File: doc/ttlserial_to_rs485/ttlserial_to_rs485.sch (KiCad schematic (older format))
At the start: 26 parts, among them J1 serial, J2 DB9_Female, SW1 term_en, U1 NE555, U2 74HC04, U3 MAX485E

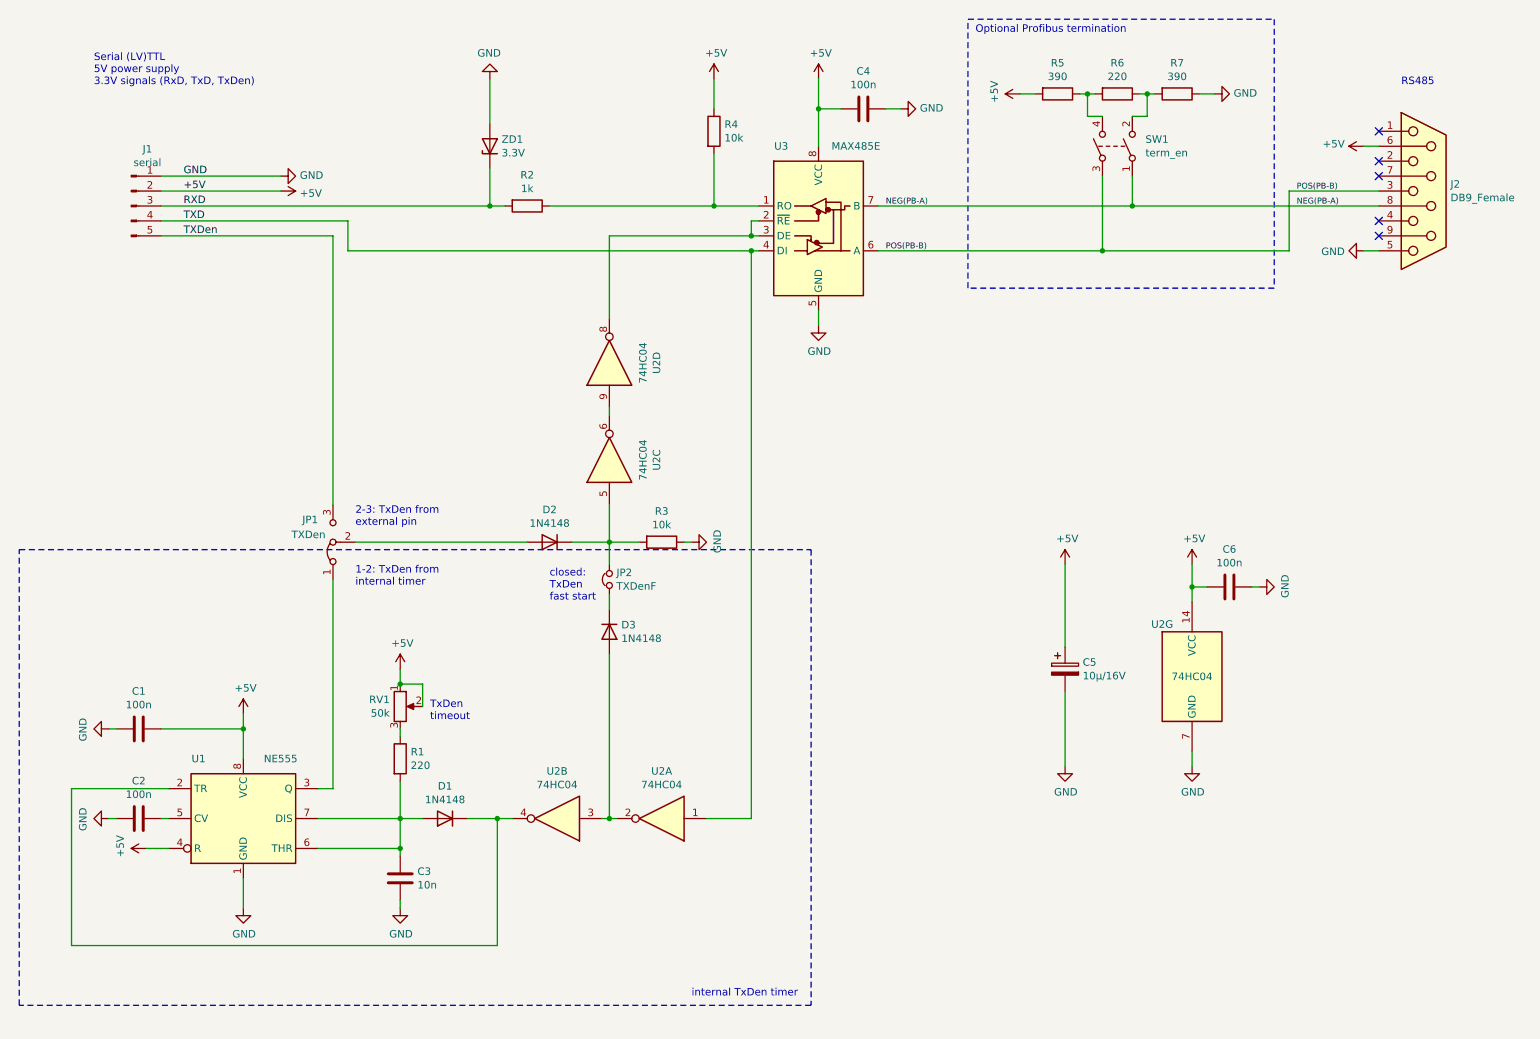
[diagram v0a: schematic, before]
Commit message: ttlserial_to_rs485: Update schematics
Signed-off-by: Michael Buesch <m@bues.ch>
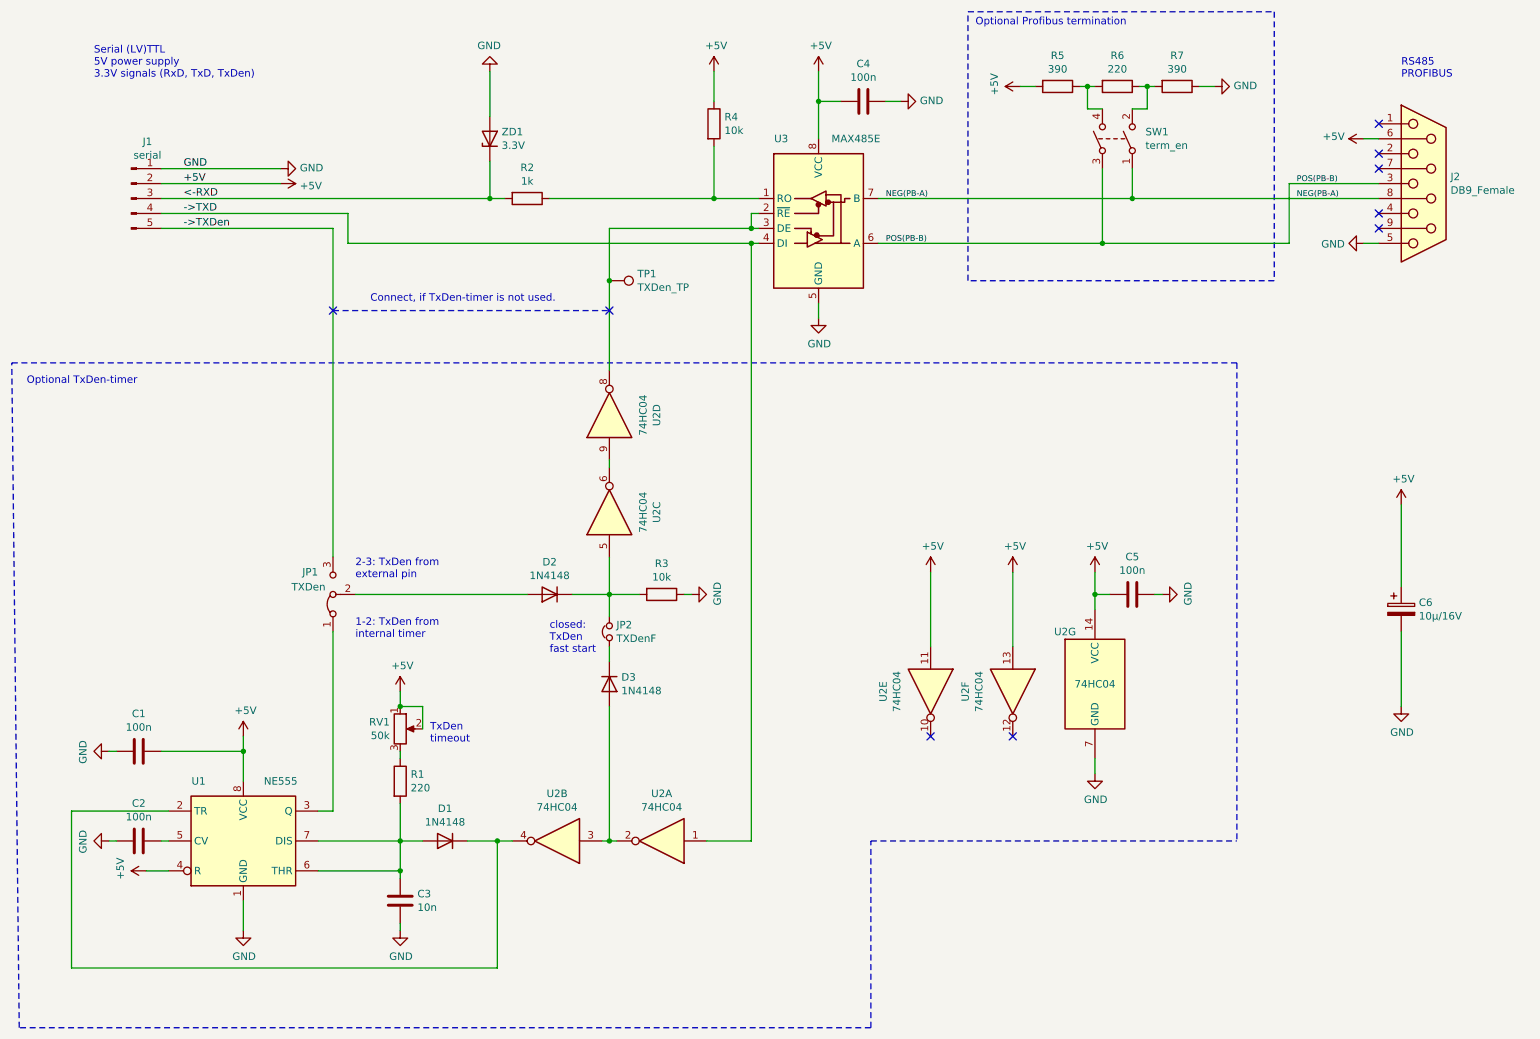
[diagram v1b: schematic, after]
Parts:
- added TP1: TXDen_TP, symbol Connector:TestPoint
- added unit 5 of U2
- added unit 6 of U2
- renumbered C6 to C5, C5 to C6
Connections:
- net +5V: now also U2.11, U2.13
- net at U2.8, U3.2 (~RE), U3.3 (DE): now also TP1.1
- net RXD renamed <-RXD
- net TXD renamed ->TXD
- net TXDen renamed ->TXDen
- no-connect marks 5 -> 9
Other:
- note added: "Connect, if TxDen-timer is not used."
- note added: "Optional TxDen-timer"
- note added: "RS485\nPROFIBUS"
- note removed: "RS485"
- note removed: "internal TxDen timer"
- moved on the sheet: C1, C2, C3, C4, C5, C6, D1, D2, D3, J1, J2, JP1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
